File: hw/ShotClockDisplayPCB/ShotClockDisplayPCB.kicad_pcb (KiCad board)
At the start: 2 copper layers, 14 parts, among them J1 PH-00041, J2 Conn_01x05_Socket, J3 Conn_01x05_Socket, J4 Conn_01x05_Socket, J5 Conn_01x05_Socket, Q4 Q_NPN_BCE, Q5 Q_PMOS_SGD, Q6 Q_NPN_BCE

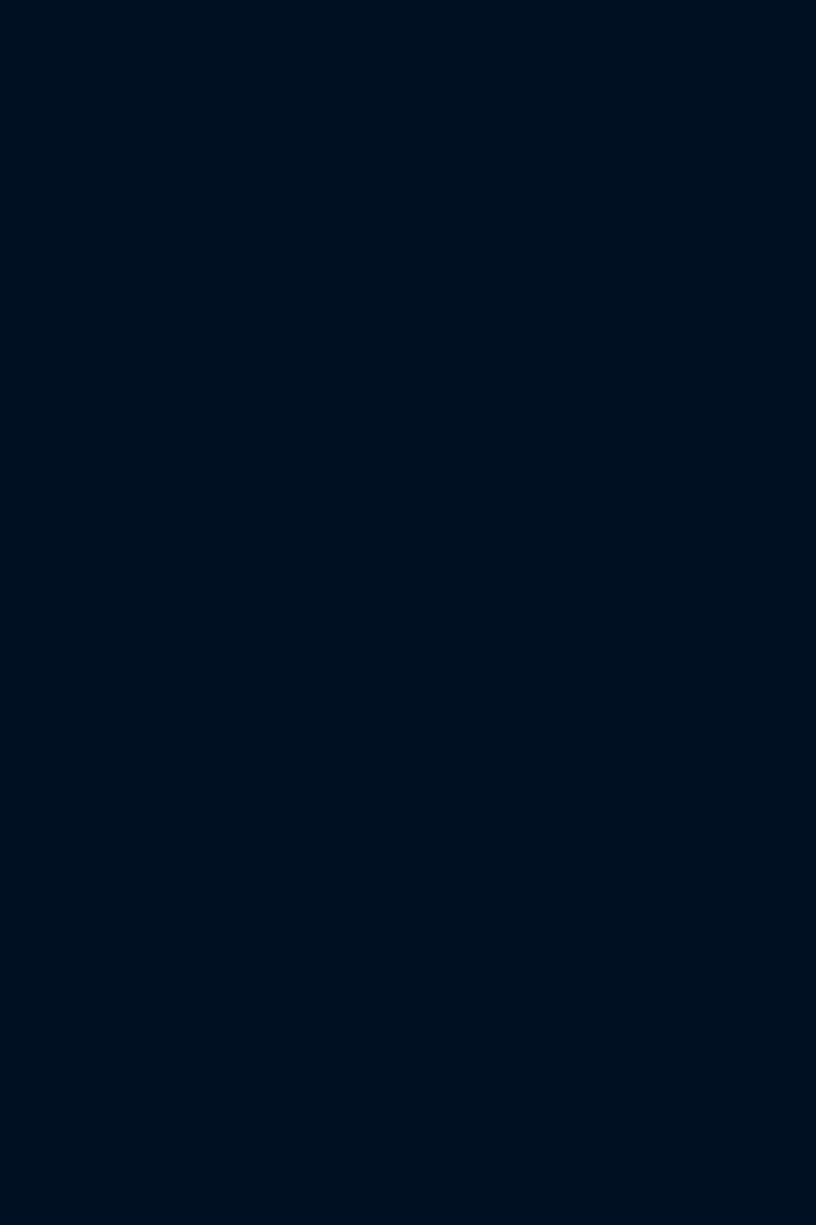
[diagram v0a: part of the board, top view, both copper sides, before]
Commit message: Finshed both schematics
- LED driving transistors are placed
- All connectors on segment display PCB are placed
- All schematic references have been re-configured (autosort on Y axis)
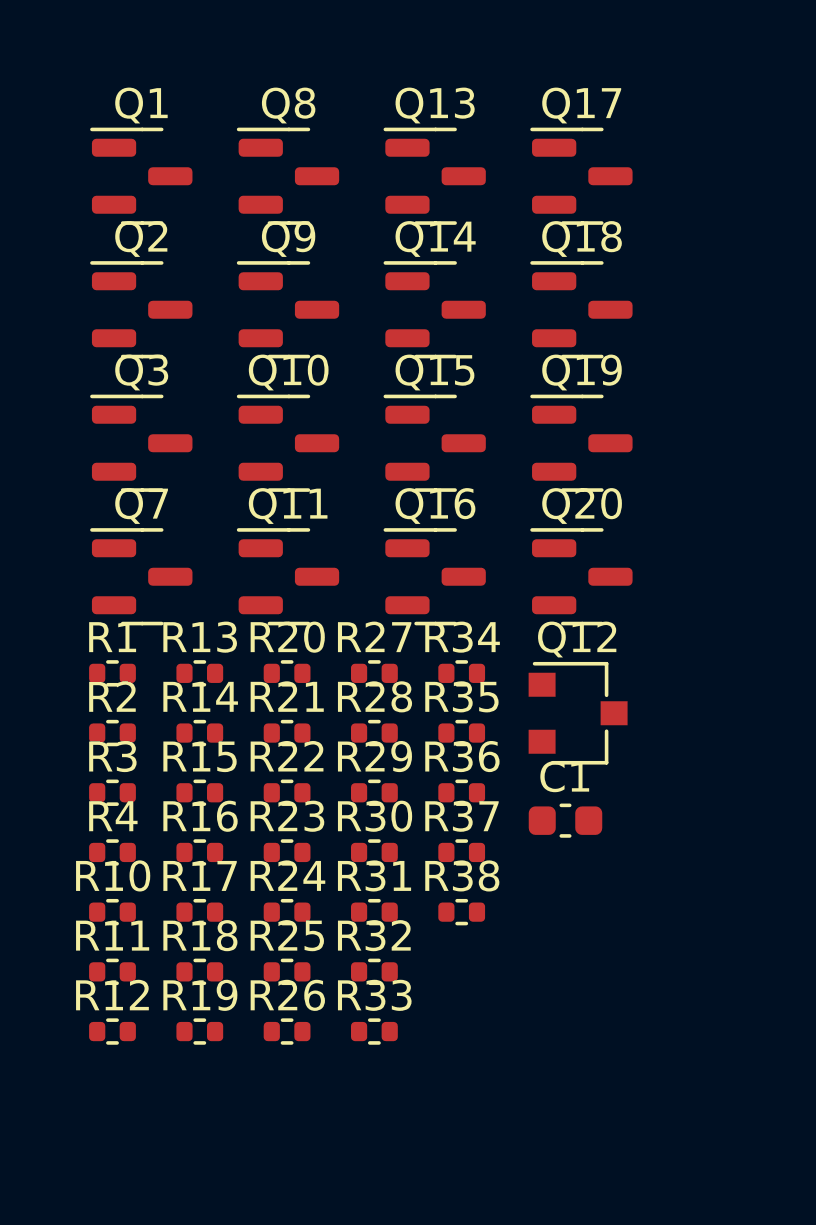
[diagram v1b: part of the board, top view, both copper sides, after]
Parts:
- added C1: 10n, Capacitor_SMD:C_0603_1608Metric, F.Cu at (69.1, 92.7)
- added Q1: Q_NPN_BCE, Package_TO_SOT_SMD:SOT-23, F.Cu at (55.0, 71.2)
- added Q10: Q_NPN_BCE, Package_TO_SOT_SMD:SOT-23, F.Cu at (59.9, 80.1)
- added Q11: Q_NPN_BCE, Package_TO_SOT_SMD:SOT-23, F.Cu at (59.9, 84.6)
- added Q12: Q_PMOS_SGD, Package_TO_SOT_SMD:SC-59, F.Cu at (69.5, 89.1)
- added Q13: Q_NPN_BCE, Package_TO_SOT_SMD:SOT-23, F.Cu at (64.7, 71.2)
- added Q14: Q_NPN_BCE, Package_TO_SOT_SMD:SOT-23, F.Cu at (64.7, 75.7)
- added Q15: Q_NPN_BCE, Package_TO_SOT_SMD:SOT-23, F.Cu at (64.7, 80.1)
- added Q16: Q_NPN_BCE, Package_TO_SOT_SMD:SOT-23, F.Cu at (64.7, 84.6)
- added Q17: Q_NPN_BCE, Package_TO_SOT_SMD:SOT-23, F.Cu at (69.6, 71.2)
- added Q18: Q_NPN_BCE, Package_TO_SOT_SMD:SOT-23, F.Cu at (69.6, 75.7)
- added Q19: Q_NPN_BCE, Package_TO_SOT_SMD:SOT-23, F.Cu at (69.6, 80.1)
- added Q2: Q_NPN_BCE, Package_TO_SOT_SMD:SOT-23, F.Cu at (55.0, 75.7)
- added Q20: Q_NPN_BCE, Package_TO_SOT_SMD:SOT-23, F.Cu at (69.6, 84.6)
- added Q3: Q_NPN_BCE, Package_TO_SOT_SMD:SOT-23, F.Cu at (55.0, 80.1)
- added Q7: Q_NPN_BCE, Package_TO_SOT_SMD:SOT-23, F.Cu at (55.0, 84.6)
- added Q8: Q_NPN_BCE, Package_TO_SOT_SMD:SOT-23, F.Cu at (59.9, 71.2)
- added Q9: Q_NPN_BCE, Package_TO_SOT_SMD:SOT-23, F.Cu at (59.9, 75.7)
- added R1: 10k, Resistor_SMD:R_0402_1005Metric, F.Cu at (54.0, 87.8)
- added R10: 10k, Resistor_SMD:R_0402_1005Metric, F.Cu at (54.0, 95.8)
- added R11: 100R, Resistor_SMD:R_0402_1005Metric, F.Cu at (54.0, 97.8)
- added R12: 10k, Resistor_SMD:R_0402_1005Metric, F.Cu at (54.0, 99.7)
- added R13: 100R, Resistor_SMD:R_0402_1005Metric, F.Cu at (56.9, 87.8)
- added R14: 10k, Resistor_SMD:R_0402_1005Metric, F.Cu at (56.9, 89.8)
- added R15: 100R, Resistor_SMD:R_0402_1005Metric, F.Cu at (56.9, 91.8)
- added R16: 10k, Resistor_SMD:R_0402_1005Metric, F.Cu at (56.9, 93.8)
- added R17: 100R, Resistor_SMD:R_0402_1005Metric, F.Cu at (56.9, 95.8)
- added R18: 10k, Resistor_SMD:R_0402_1005Metric, F.Cu at (56.9, 97.8)
- added R19: 100R, Resistor_SMD:R_0402_1005Metric, F.Cu at (56.9, 99.7)
- added R2: 100R, Resistor_SMD:R_0402_1005Metric, F.Cu at (54.0, 89.8)
- added R20: 1k, Resistor_SMD:R_0402_1005Metric, F.Cu at (59.8, 87.8)
- added R21: 10k, Resistor_SMD:R_0402_1005Metric, F.Cu at (59.8, 89.8)
- added R22: 100k, Resistor_SMD:R_0402_1005Metric, F.Cu at (59.8, 91.8)
- added R23: 10k, Resistor_SMD:R_0402_1005Metric, F.Cu at (59.8, 93.8)
- added R24: 10k, Resistor_SMD:R_0402_1005Metric, F.Cu at (59.8, 95.8)
- added R25: 100R, Resistor_SMD:R_0402_1005Metric, F.Cu at (59.8, 97.8)
- added R26: 100R, Resistor_SMD:R_0402_1005Metric, F.Cu at (59.8, 99.7)
- added R27: 10k, Resistor_SMD:R_0402_1005Metric, F.Cu at (62.7, 87.8)
- added R28: 10k, Resistor_SMD:R_0402_1005Metric, F.Cu at (62.7, 89.8)
- added R29: 100R, Resistor_SMD:R_0402_1005Metric, F.Cu at (62.7, 91.8)
- added R3: 10k, Resistor_SMD:R_0402_1005Metric, F.Cu at (54.0, 91.8)
- added R30: 100R, Resistor_SMD:R_0402_1005Metric, F.Cu at (62.7, 93.8)
- added R31: 10k, Resistor_SMD:R_0402_1005Metric, F.Cu at (62.7, 95.8)
- added R32: 10k, Resistor_SMD:R_0402_1005Metric, F.Cu at (62.7, 97.8)
- added R33: 100R, Resistor_SMD:R_0402_1005Metric, F.Cu at (62.7, 99.7)
- added R34: 100R, Resistor_SMD:R_0402_1005Metric, F.Cu at (65.6, 87.8)
- added R35: 10k, Resistor_SMD:R_0402_1005Metric, F.Cu at (65.6, 89.8)
- added R36: 10k, Resistor_SMD:R_0402_1005Metric, F.Cu at (65.6, 91.8)
- added R37: 100R, Resistor_SMD:R_0402_1005Metric, F.Cu at (65.6, 93.8)
- added R38: 100R, Resistor_SMD:R_0402_1005Metric, F.Cu at (65.6, 95.8)
- added R4: 100R, Resistor_SMD:R_0402_1005Metric, F.Cu at (54.0, 93.8)
- R5: value ? -> 10k
- R6: value ? -> 100R
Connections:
- net +3.3V renamed +5V
- net /LED Driving Transistors/PWM1_V renamed /LED Driving Transistors/PWM1_5V
- J2 pad 2: /Segment Display Connectors/SEG1_E -> /LED Driving Transistors/OUT_DISP2_SEG_E
- J2 pad 3: /Segment Display Connectors/SEG1_D -> /LED Driving Transistors/OUT_DISP1_SEG_D
- J2 pad 4: /Segment Display Connectors/SEG1_C -> /LED Driving Transistors/OUT_DISP1_SEG_C
- J3 pad 1: /Segment Display Connectors/SEG1_B -> /LED Driving Transistors/OUT_DISP1_SEG_B
- J3 pad 3: /Segment Display Connectors/SEG1_DP -> /LED Driving Transistors/OUT_DISP1_SEG_DP
- J3 pad 4: /Segment Display Connectors/SEG1_F -> /LED Driving Transistors/OUT_DISP1_SEG_F
- J3 pad 5: /Segment Display Connectors/SEG1_G -> /LED Driving Transistors/OUT_DISP1_SEG_G
- J4 pad 2: /Segment Display Connectors/SEG2_E -> /LED Driving Transistors/OUT_DISP1_SEG_E
- J4 pad 3: /Segment Display Connectors/SEG2_D -> /LED Driving Transistors/OUT_DISP2_SEG_D
- J4 pad 4: /Segment Display Connectors/SEG2_C -> /LED Driving Transistors/OUT_DISP2_SEG_C
- J5 pad 1: /Segment Display Connectors/SEG2_B -> /LED Driving Transistors/OUT_DISP2_SEG_B
- J5 pad 2: /Segment Display Connectors/SEG2_A -> /LED Driving Transistors/OUT_DISP2_SEG_A
- J5 pad 3: /Segment Display Connectors/SEG2_DP -> /LED Driving Transistors/OUT_DISP2_SEG_DP
- J5 pad 4: /Segment Display Connectors/SEG2_F -> /LED Driving Transistors/OUT_DISP2_SEG_F
- J5 pad 5: /Segment Display Connectors/SEG2_G -> /LED Driving Transistors/OUT_DISP2_SEG_G
- Q4 pad 3: unconnected-(Q4-E-Pad3) -> GND

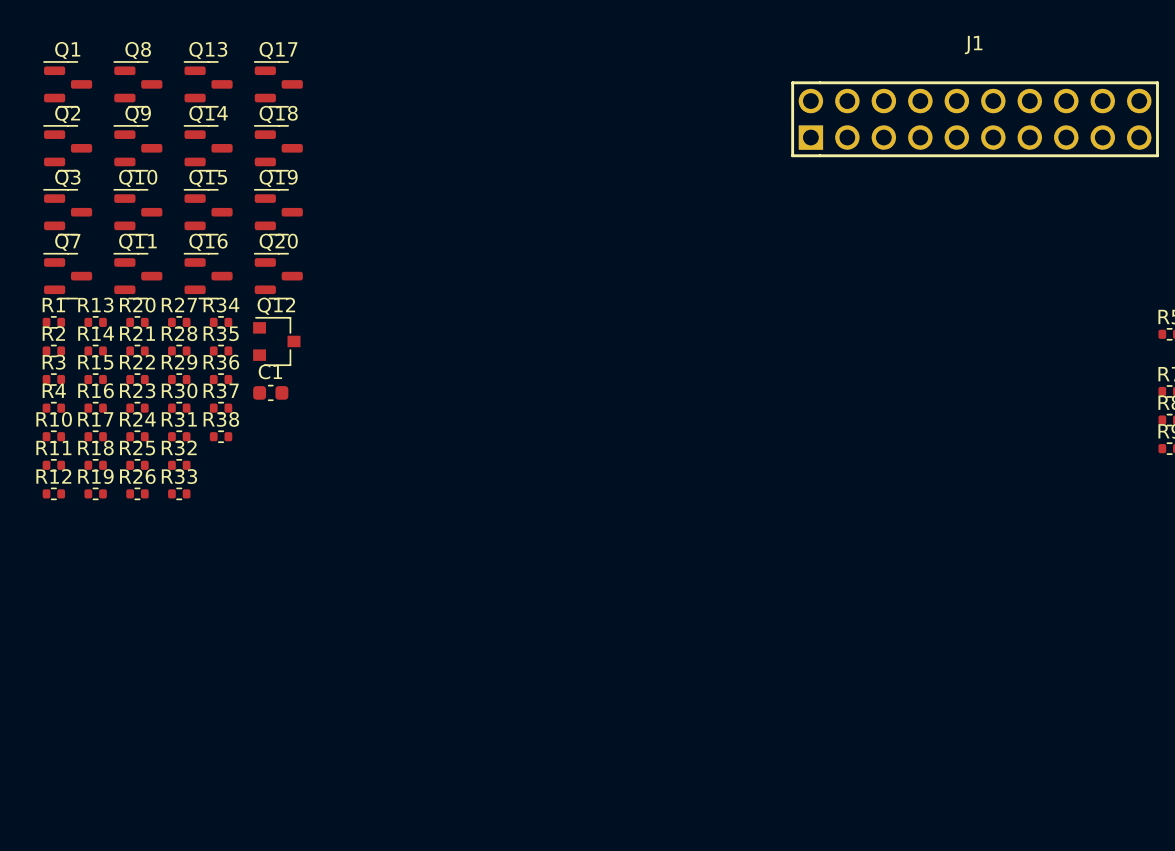
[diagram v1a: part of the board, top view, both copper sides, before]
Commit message: Moved components around
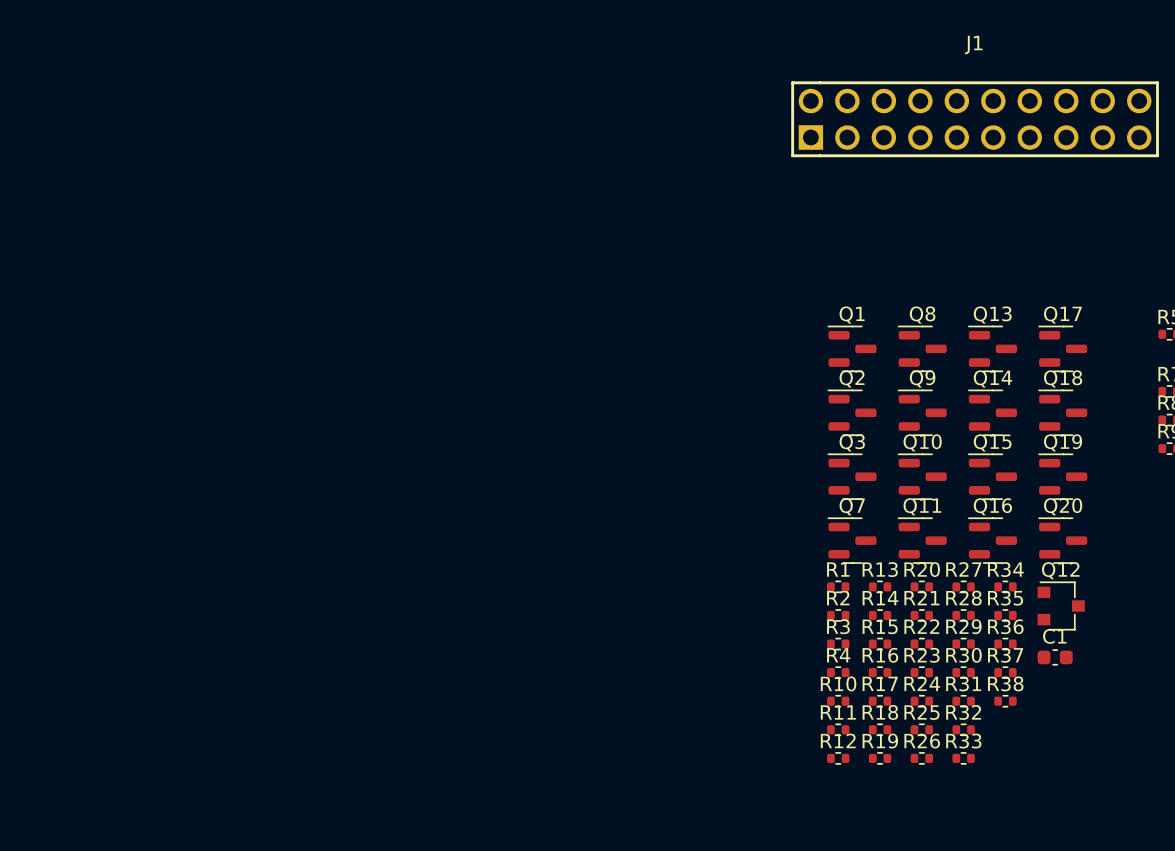
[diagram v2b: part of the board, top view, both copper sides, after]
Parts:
- moved Q10 57.6 mm to (114.5, 98.5)
- moved Q11 57.6 mm to (114.5, 103.0)
- moved R13 57.6 mm to (111.5, 106.2)
- moved R16 57.6 mm to (111.5, 112.2)
- moved R18 57.6 mm to (111.5, 116.2)
- moved R19 57.6 mm to (111.5, 118.2)
- moved C1 57.6 mm to (123.7, 111.1)
- moved Q12 57.6 mm to (124.1, 107.5)
- moved Q15 57.6 mm to (119.4, 98.5)
- moved Q16 57.6 mm to (119.4, 103.0)
- moved Q19 57.6 mm to (124.2, 98.5)
- moved Q20 57.6 mm to (124.2, 103.0)
- moved Q3 57.6 mm to (109.6, 98.5)
- moved Q7 57.6 mm to (109.6, 103.0)
- moved R20 57.6 mm to (114.4, 106.2)
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
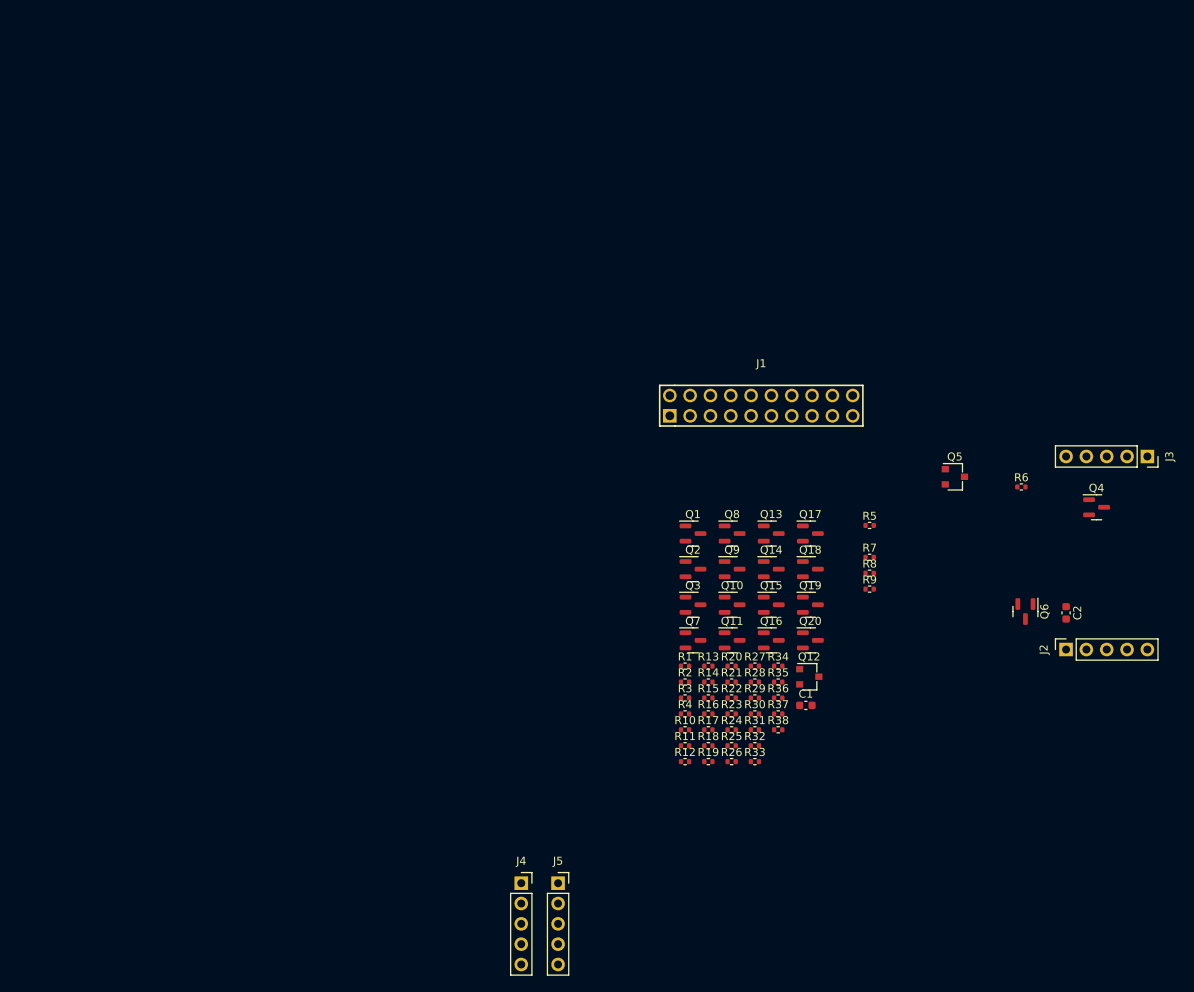
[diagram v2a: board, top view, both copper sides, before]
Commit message: Added outloiuns to the display print
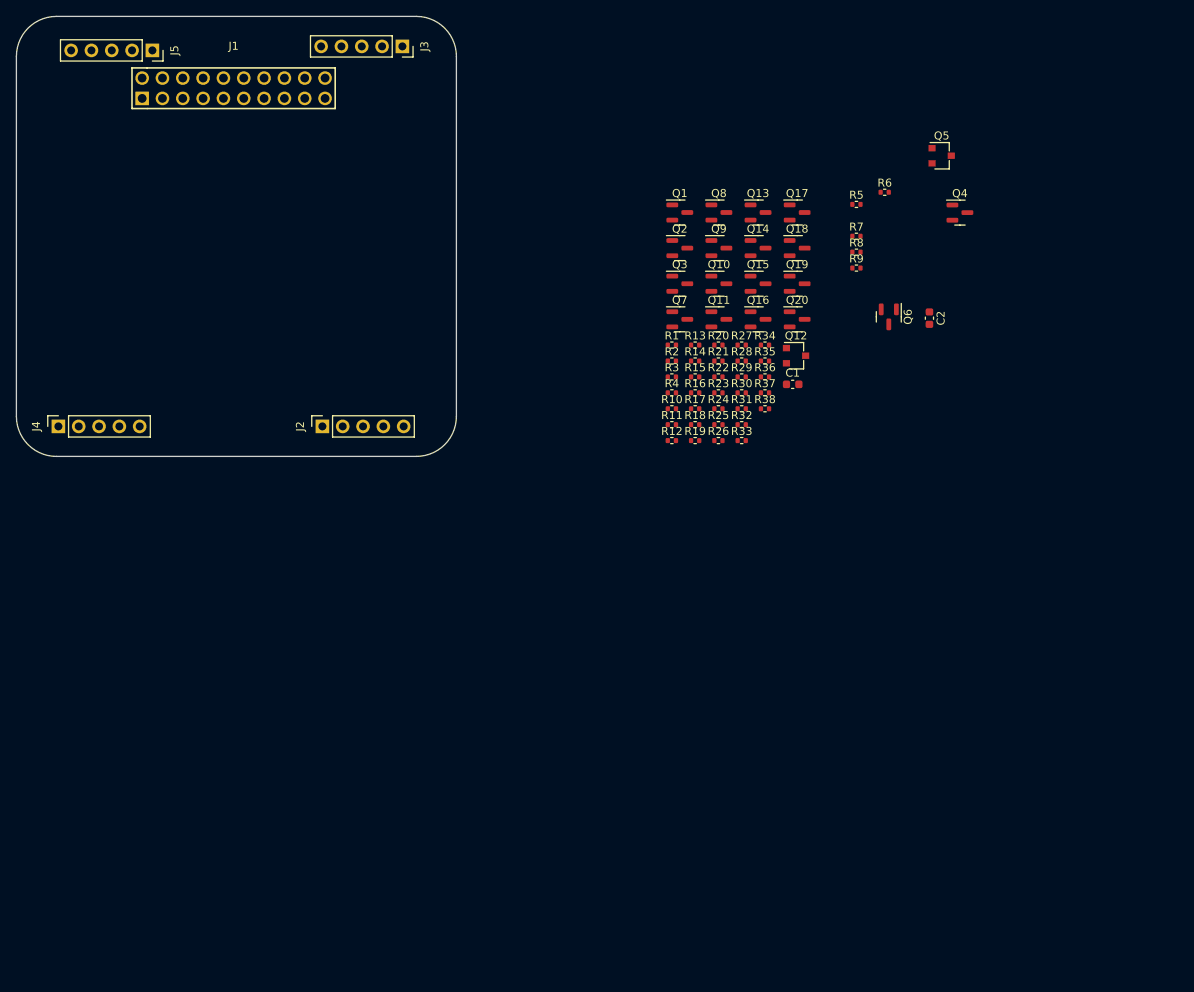
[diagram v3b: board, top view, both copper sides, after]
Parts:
- moved J5 115.8 mm to (42.0, 29.2), turned to -90 degrees
- moved J3 106.3 mm to (73.2, 28.8)
- moved J2 97.1 mm to (63.2, 76.2)
- moved J4 81.3 mm to (30.2, 76.2), turned to 90 degrees
- moved J1 77.0 mm to (52.1, 34.0)
- moved C2 40.6 mm to (139.1, 62.7)
- moved Q4 40.6 mm to (142.9, 49.5)
- moved R6 40.6 mm to (133.5, 47.0)
- moved Q6 40.6 mm to (134.1, 62.6)
- moved R1 40.2 mm to (106.9, 66.1)
- moved R11 40.2 mm to (106.9, 76.0)
- moved R13 40.2 mm to (109.8, 66.1)
- moved R18 40.2 mm to (109.8, 76.0)
- moved R20 40.2 mm to (112.8, 66.1)
- moved R25 40.2 mm to (112.8, 76.0)
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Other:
- board outline added: 55 x 55 mm
